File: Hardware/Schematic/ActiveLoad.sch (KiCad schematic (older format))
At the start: 74 parts, among them P1 USB_B, P2 Banana jacks, P3 AKL 101-2, P4 TC2030-CTX, Q1 BTS117, SW1 FSMSM, SW2 ESP4020, U1 MAX3207E, U2 STM32F072C8, U3 DS18B20, U4 MCP6002, U5 LM317AEMP, U6 LM9036M-3.3, X1 CSTCE8M00G15

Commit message: updated schematic PCB work
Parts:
- removed P1: USB_B, Connect:USB_Mini-B, symbol USB_B
- added C26: 100n/50V, Capacitors_SMD:C_0805, symbol C
- added P1: USB_OTG, Connect:USB_Mini-B, symbol USB_OTG
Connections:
- net ENC_SW: now also U2.12 (USART2_TX/ADC1_IN2/TIM2_CH3/TIM15_CH1/PA2); no longer U2.15 (SPI1_SCK/I2S1_CK/TIM2_CH1_ETR/ADC1_IN5/DAC2/PA5)
- net GND: now also C26.1
- net USB_D+: now also P1.3 (D+)
- net USB_D-: now also P1.2 (D-)
- net at U2.18 (ADC1_IN8/TIM3_CH3/TIM1_CH2N/EVENTOUT/USART3_CK/PB0): now also R22.1
- net at FB2.1: now also P1.1 (VCC)
- net at FB1.1: now also P1.5 (GND)
- net at C1.1, R1.2: now also P1.6 (shield)
- net at R23.1, U5.3 (IN): now also C26.2
- no-connect marks 22 -> 21
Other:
- moved on the sheet: D1, FB1, R22
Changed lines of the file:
@@
 $EndDescr
-$Comp
-L STM32F072CB U2
-U 1 1 569BF24D
-P 3950 4750
-F 0 "U2" H 2450 6650 60  0000 C CNN
-F 1 "STM32F072C8" H 5200 2850 60  0000 C CNN
-F 2 "Housings_QFP:LQFP-48_7x7mm_Pitch0.5mm" H 3950 4750 40  0001 C CIN
-F 3 "" H 3950 4750 60  0000 C CNN
-	1    3950 4750
-	1    0    0    -1
-$EndComp
 $Comp
 L BTS117 Q1
@@
 	1    0    0    -1
 $EndComp
-$Comp
-L USB_B P1
-U 1 1 56A64375
-P 1100 1350
-F 0 "P1" H 1300 1150 50  0000 C CNN
-F 1 "USB_B" H 1050 1550 50  0000 C CNN
-F 2 "Connect:USB_Mini-B" V 1050 1250 50  0001 C CNN
-F 3 "" V 1050 1250 50  0000 C CNN
-	1    1100 1350
-	0    -1   1    0
-$EndComp
-Text Notes 1300 1000 2    60   ~ 0
+Text Notes 1050 800  2    60   ~ 0
 Mini USB
 $Comp
@@
 L FILTER FB1
 U 1 1 56A649C1
-P 1600 1900
-F 0 "FB1" H 1600 2050 50  0000 C CNN
-F 1 "8,2µH/0805" H 1600 1800 50  0000 C CNN
-F 2 "Resistors_SMD:R_0805" H 1600 1900 50  0001 C CNN
-F 3 "" H 1600 1900 50  0000 C CNN
-	1    1600 1900
+P 1600 1950
+F 0 "FB1" H 1600 2100 50  0000 C CNN
+F 1 "8,2µH/0805" H 1600 1850 50  0000 C CNN
+F 2 "Resistors_SMD:R_0805" H 1600 1950 50  0001 C CNN
+F 3 "" H 1600 1950 50  0000 C CNN
+	1    1600 1950
 	0    1    1    0
 $EndComp
@@
 L LED D1
 U 1 1 56A46305
-P 12150 5850
-F 0 "D1" H 12150 5950 50  0000 C CNN
-F 1 "Run LED green" H 12150 5750 50  0000 C CNN
-F 2 "LEDs:LED_0603" H 12150 5850 50  0001 C CNN
-F 3 "" H 12150 5850 50  0000 C CNN
-	1    12150 5850
+P 6200 5450
+F 0 "D1" H 6200 5550 50  0000 C CNN
+F 1 "Run LED green" H 6200 5350 50  0000 C CNN
+F 2 "LEDs:LED_0603" H 6200 5450 50  0001 C CNN
+F 3 "" H 6200 5450 50  0000 C CNN
+	1    6200 5450
 	0    -1   -1   0
 $EndComp
@@
 L R R22
 U 1 1 56A46428
-P 12150 5350
-F 0 "R22" V 12230 5350 50  0000 C CNN
-F 1 "220" V 12150 5350 50  0000 C CNN
-F 2 "Resistors_SMD:R_0603" V 12080 5350 50  0001 C CNN
-F 3 "" H 12150 5350 50  0000 C CNN
-	1    12150 5350
+P 6200 5050
+F 0 "R22" V 6280 5050 50  0000 C CNN
+F 1 "220" V 6200 5050 50  0000 C CNN
+F 2 "Resistors_SMD:R_0603" V 6130 5050 50  0001 C CNN
+F 3 "" H 6200 5050 50  0000 C CNN
+	1    6200 5050
 	1    0    0    -1
 $EndComp
@@
 L GND #PWR016
 U 1 1 56A47C47
-P 12150 6200
-F 0 "#PWR016" H 12150 5950 50  0001 C CNN
-F 1 "GND" H 12150 6050 50  0000 C CNN
-F 2 "" H 12150 6200 50  0000 C CNN
-F 3 "" H 12150 6200 50  0000 C CNN
-	1    12150 6200
+P 6200 5700
+F 0 "#PWR016" H 6200 5450 50  0001 C CNN
+F 1 "GND" H 6200 5550 50  0000 C CNN
+F 2 "" H 6200 5700 50  0000 C CNN
+F 3 "" H 6200 5700 50  0000 C CNN
+	1    6200 5700
 	1    0    0    -1
 $EndComp
@@
 Text GLabel 6100 3850 2    47   Input ~ 0
 ENC_B
-Text GLabel 6100 3650 2    47   Input ~ 0
+Text GLabel 6050 3350 2    47   Input ~ 0
 ENC_SW
 $Comp
@@
 Text GLabel 5200 1350 0    47   BiDi ~ 0
 TEMP
-Text GLabel 6350 5100 0    47   BiDi ~ 0
+Text GLabel 7650 6100 0    47   BiDi ~ 0
 TEMP
-Text Notes 6150 5250 0    79   ~ 0
+Text Notes 7450 6250 0    79   ~ 0
 TBD
 Text Notes 6200 800  0    79   ~ 0
@@
 Wire Wire Line
 	750  1800 1000 1800
-Wire Wire Line
-	1000 1650 1000 1900
 Connection ~ 1000 1800
 Wire Wire Line
@@
 	750  2300 1600 2300
 Wire Wire Line
-	1600 2250 1600 2400
+	1600 2300 1600 2400
 Connection ~ 1600 2300
 Wire Wire Line
@@
 Connection ~ 1000 2300
 Wire Wire Line
-	1400 1450 1600 1450
-Wire Wire Line
-	1600 1450 1600 1550
-Wire Wire Line
 	2950 1300 3050 1300
 Wire Wire Line
@@
 	6050 4450 5650 4450
 Wire Wire Line
-	12150 5500 12150 5650
-Wire Wire Line
-	12150 6050 12150 6200
+	6200 5200 6200 5250
+Wire Wire Line
+	6200 5650 6200 5700
 Wire Wire Line
 	1700 3300 2250 3300
@@
 	9100 1600 9000 1600
 Wire Wire Line
-	9000 1600 9000 2200
-Wire Wire Line
-	9000 2200 7800 2200
+	9000 2200 9000 1600
+Wire Wire Line
+	7800 2200 9000 2200
 Wire Wire Line
 	8750 1350 8750 1250
@@
 Connection ~ 9900 4450
 Wire Wire Line
-	6100 3650 5650 3650
-Wire Wire Line
 	6100 3750 5650 3750
 Wire Wire Line
@@
 	1000 6650 1000 6800
 Wire Wire Line
-	1100 6800 1100 6750
-Wire Wire Line
-	1100 6750 850  6750
+	1100 6750 1100 6800
+Wire Wire Line
+	850  6750 1100 6750
 Connection ~ 1000 6750
 Wire Wire Line
@@
 Connection ~ 850  5700
 Wire Wire Line
-	8900 4100 8850 4100
+	8600 4100 8900 4100
 Wire Wire Line
 	9700 4100 9800 4100
@@
 	9300 4900 9300 4850
 Connection ~ 9300 4500
-Text Notes 7850 4200 0    60   ~ 0
+Text Notes 7450 4100 0    60   ~ 0
 Alternative regulator\nFit EITHER U5 or U6
 $Comp
@@
 NoConn ~ 2250 5550
 NoConn ~ 5650 3250
-NoConn ~ 5650 3350
 NoConn ~ 5650 3450
 NoConn ~ 5650 3950
 NoConn ~ 5650 4050
 NoConn ~ 5650 4150
-NoConn ~ 5650 4850
 NoConn ~ 5650 4950
 NoConn ~ 5650 5050
@@
 	1    0    0    -1
 $EndComp
+$Comp
+L USB_OTG P1
+U 1 1 56B5FBE1
+P 1100 1350
+F 0 "P1" H 1425 1225 50  0000 C CNN
+F 1 "USB_OTG" H 1100 1550 50  0000 C CNN
+F 2 "Connect:USB_Mini-B" V 1050 1250 50  0001 C CNN
+F 3 "" V 1050 1250 50  0000 C CNN
+	1    1100 1350
+	0    -1   1    0
+$EndComp
+NoConn ~ 1400 1450
+Wire Wire Line
+	1000 1750 1000 1900
+Wire Wire Line
+	1400 1550 1600 1550
+Wire Wire Line
+	1600 1550 1600 1600
+$Comp
+L C C26
+U 1 1 56B68873
+P 8600 4300
+F 0 "C26" H 8625 4400 50  0000 L CNN
+F 1 "100n/50V" H 8625 4200 50  0000 L CNN
+F 2 "Capacitors_SMD:C_0805" H 8638 4150 50  0001 C CNN
+F 3 "" H 8600 4300 50  0000 C CNN
+	1    8600 4300
+	-1   0    0    1
+$EndComp
+$Comp
+L GND #PWR053
+U 1 1 56B689E5
+P 8600 4550
+F 0 "#PWR053" H 8600 4300 50  0001 C CNN
+F 1 "GND" H 8600 4400 50  0000 C CNN
+F 2 "" H 8600 4550 50  0000 C CNN
+F 3 "" H 8600 4550 50  0000 C CNN
+	1    8600 4550
+	1    0    0    -1
+$EndComp
+Wire Wire Line
+	8600 4550 8600 4450
+Wire Wire Line
+	8600 4150 8600 4100
+Connection ~ 8850 4100
+$Comp
+L STM32F072CB U2
+U 1 1 569BF24D
+P 3950 4750
+F 0 "U2" H 2450 6650 60  0000 C CNN
+F 1 "STM32F072C8" H 5200 2850 60  0000 C CNN
+F 2 "Housings_QFP:LQFP-48_7x7mm_Pitch0.5mm" H 3950 4750 40  0001 C CIN
+F 3 "" H 3950 4750 60  0000 C CNN
+	1    3950 4750
+	1    0    0    -1
+$EndComp
+Wire Wire Line
+	6050 3350 5650 3350
+Wire Wire Line
+	5650 4850 6200 4850
+Wire Wire Line
+	6200 4850 6200 4900
 $EndSCHEMATC

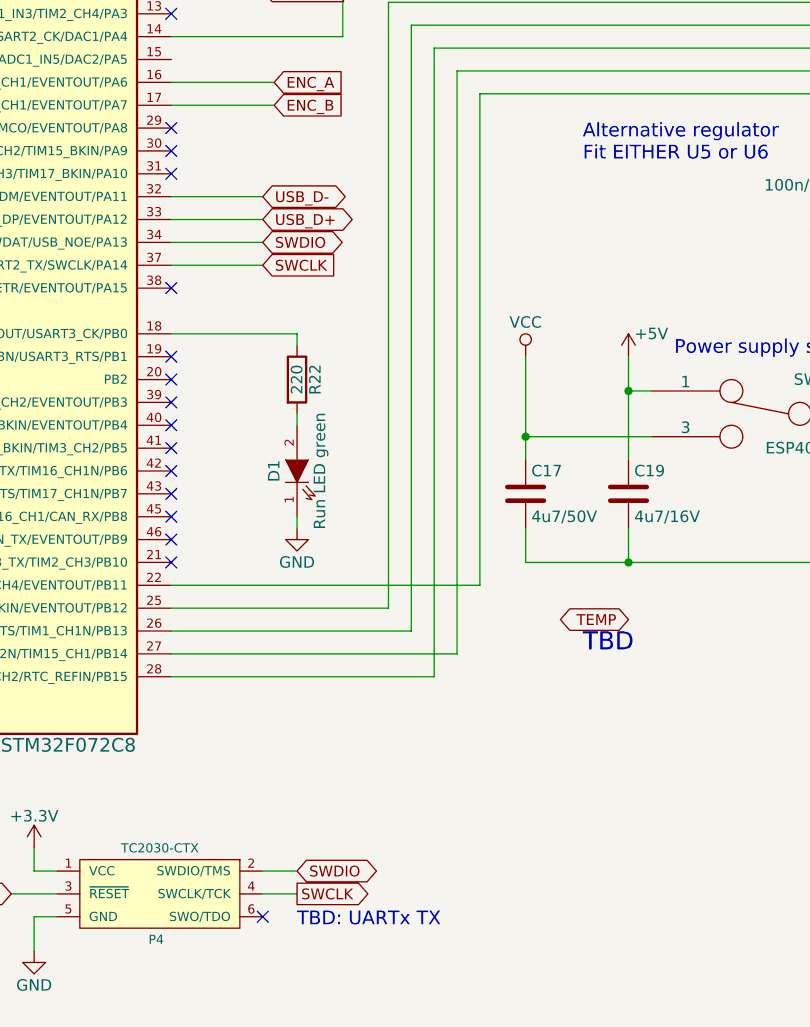
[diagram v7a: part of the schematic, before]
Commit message: updated schematic (TEMP pin and LED pin) finished PCB
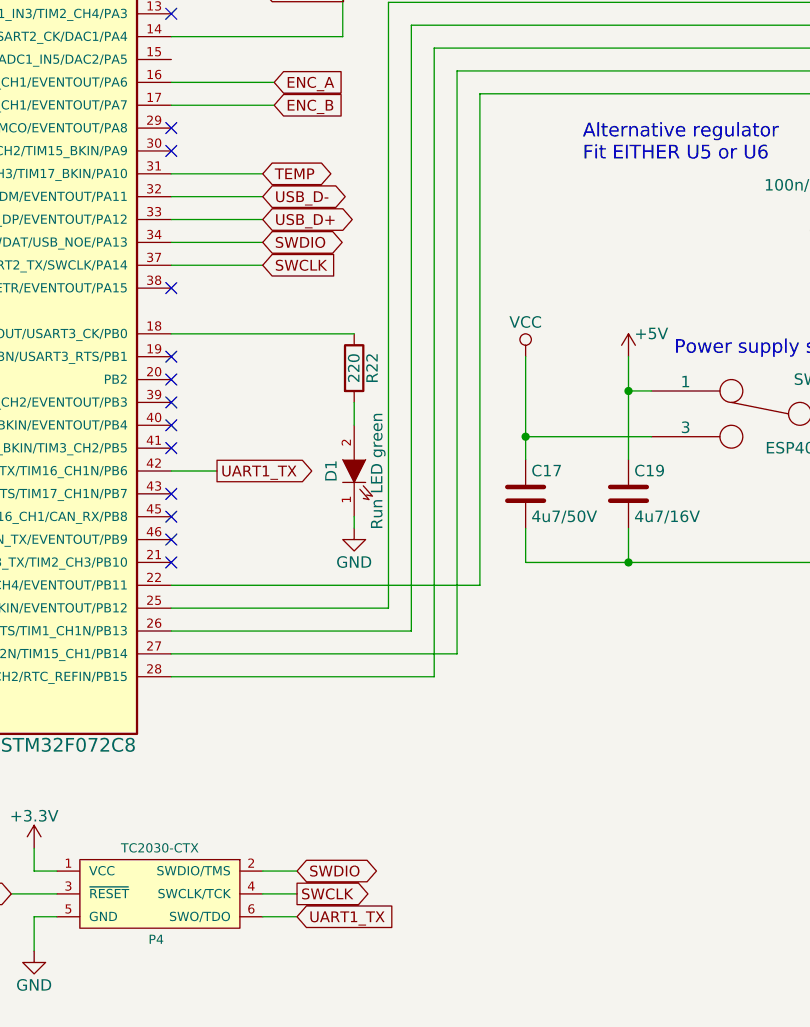
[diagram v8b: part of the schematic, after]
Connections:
- net TEMP: now also U2.31 (USART1_RX/TIM1_CH3/TIM17_BKIN/PA10)
- net UART1_TX: now reaches U2.42 (I2C1_SCL/USART1_TX/TIM16_CH1N/PB6)
- net UART1_TX: now also P4.6 (SWO/TDO)
- no-connect marks 21 -> 18
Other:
- note removed: "TBD"
- note removed: "TBD: UARTx TX"
- moved on the sheet: D1, R22
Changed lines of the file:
@@
 Text GLabel 6200 7300 2    47   Output ~ 0
 SWCLK
-NoConn ~ 6050 7400
 $Comp
 L R R4
@@
 L LED D1
 U 1 1 56A46305
-P 6200 5450
-F 0 "D1" H 6200 5550 50  0000 C CNN
-F 1 "Run LED green" H 6200 5350 50  0000 C CNN
-F 2 "LEDs:LED_0603" H 6200 5450 50  0001 C CNN
-F 3 "" H 6200 5450 50  0000 C CNN
-	1    6200 5450
+P 6450 5450
+F 0 "D1" H 6450 5550 50  0000 C CNN
+F 1 "Run LED green" H 6450 5350 50  0000 C CNN
+F 2 "LEDs:LED_0603" H 6450 5450 50  0001 C CNN
+F 3 "" H 6450 5450 50  0000 C CNN
+	1    6450 5450
 	0    -1   -1   0
 $EndComp
@@
 L R R22
 U 1 1 56A46428
-P 6200 5050
-F 0 "R22" V 6280 5050 50  0000 C CNN
-F 1 "220" V 6200 5050 50  0000 C CNN
-F 2 "Resistors_SMD:R_0603" V 6130 5050 50  0001 C CNN
-F 3 "" H 6200 5050 50  0000 C CNN
-	1    6200 5050
+P 6450 5000
+F 0 "R22" V 6530 5000 50  0000 C CNN
+F 1 "220" V 6450 5000 50  0000 C CNN
+F 2 "Resistors_SMD:R_0603" V 6380 5000 50  0001 C CNN
+F 3 "" H 6450 5000 50  0000 C CNN
+	1    6450 5000
 	1    0    0    -1
 $EndComp
@@
 L GND #PWR016
 U 1 1 56A47C47
-P 6200 5700
-F 0 "#PWR016" H 6200 5450 50  0001 C CNN
-F 1 "GND" H 6200 5550 50  0000 C CNN
-F 2 "" H 6200 5700 50  0000 C CNN
-F 3 "" H 6200 5700 50  0000 C CNN
-	1    6200 5700
+P 6450 5700
+F 0 "#PWR016" H 6450 5450 50  0001 C CNN
+F 1 "GND" H 6450 5550 50  0000 C CNN
+F 2 "" H 6450 5700 50  0000 C CNN
+F 3 "" H 6450 5700 50  0000 C CNN
+	1    6450 5700
 	1    0    0    -1
 $EndComp
@@
 Text GLabel 6050 4350 2    47   BiDi ~ 0
 USB_D+
-Text Notes 6200 7450 0    60   ~ 0
-TBD: UARTx TX
 $Comp
 L FILTER FB2
@@
 Text GLabel 5200 1350 0    47   BiDi ~ 0
 TEMP
-Text GLabel 7650 6100 0    47   BiDi ~ 0
+Text GLabel 6050 4150 2    47   BiDi ~ 0
 TEMP
-Text Notes 7450 6250 0    79   ~ 0
-TBD
 Text Notes 6200 800  0    79   ~ 0
 Thermally connect\nU3 to FET!
@@
 	6050 4450 5650 4450
 Wire Wire Line
-	6200 5200 6200 5250
-Wire Wire Line
-	6200 5650 6200 5700
+	6450 5150 6450 5250
+Wire Wire Line
+	6450 5650 6450 5700
 Wire Wire Line
 	1700 3300 2250 3300
@@
 NoConn ~ 5650 3950
 NoConn ~ 5650 4050
-NoConn ~ 5650 4150
 NoConn ~ 5650 4950
 NoConn ~ 5650 5050
@@
 NoConn ~ 5650 5250
 NoConn ~ 5650 5350
-NoConn ~ 5650 5450
 NoConn ~ 5650 5550
 NoConn ~ 5650 5650
@@
 	6050 3350 5650 3350
 Wire Wire Line
-	5650 4850 6200 4850
-Wire Wire Line
-	6200 4850 6200 4900
+	5650 4850 6450 4850
+Wire Wire Line
+	6050 4150 5650 4150
+Text GLabel 6200 7400 2    47   Input ~ 0
+UART1_TX
+Wire Wire Line
+	6200 7400 6050 7400
+Text GLabel 5850 5450 2    47   Output ~ 0
+UART1_TX
+Wire Wire Line
+	5650 5450 5850 5450
 $EndSCHEMATC
